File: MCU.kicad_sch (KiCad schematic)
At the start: 18 parts, among them U2 LTV-817, U3 LTV-817, Y1 TXC 7R-32.000MEEV-T

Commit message: Dodanie footprintów
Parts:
- added C11: 0.8pF, Capacitor_SMD:C_0201_0603Metric, symbol Device:C
- added C15: 0.3pF, Capacitor_SMD:C_0201_0603Metric, symbol Device:C
- added FL1: DLF162500LT-5028A1, Sterownik_roletyLibrary:DLF162500LT5028A1, symbol DLF162500LT-5028A1:DLF162500LT-5028A1
- added L1: 2.7nH, Inductor_SMD:L_0201_0603Metric, symbol Device:L
- 111111111: renamed from 1111111; footprint (none) -> Sterownik_roletyLibrary:QFN50P500X500X60-33N-D; symbol STM32WBA50KGU6:STM32WBA54KGU6 -> STM32WBA54KGU6:STM32WBA54KGU6
- C1, C10, C2, C3, C4, C5, C6, C7, C8, C9: footprint (none) -> Capacitor_SMD:C_0201_0603Metric
- C12: renamed from C11; footprint (none) -> Capacitor_SMD:C_0201_0603Metric
- C13: renamed from C12; footprint (none) -> Capacitor_SMD:C_0201_0603Metric
- C14: renamed from C13; footprint (none) -> Capacitor_SMD:C_0201_0603Metric
- Y1: footprint (none) -> Sterownik_roletyLibrary:TXC 7R-32.000MEEV-T
- renumbered U2 to U1, U3 to U2
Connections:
- net GND: now also C11.2, C15.2, FL1.2 (GND_1), FL1.4 (GND_2)
- net at 111111111.25 (RF): now also C11.1, L1.1; no longer AE1.1 (A)
- net Switch_Input_1 renamed Switch_input_1
- new net: C15.1, FL1.1 (IN), L1.2
- new net: AE1.1 (A), FL1.3 (OUT)
- no-connect marks 11 -> 13
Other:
- moved on the sheet: AE1, C12, C13, C14, Y1

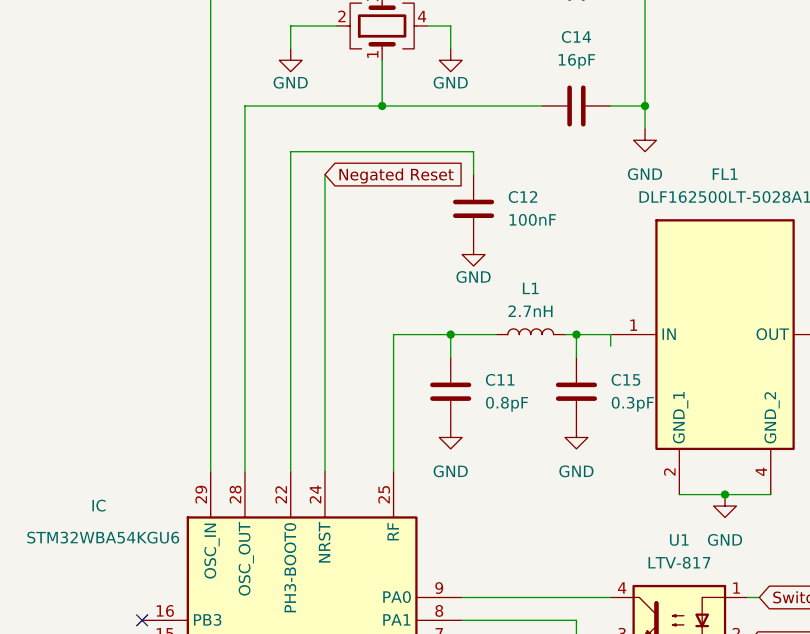
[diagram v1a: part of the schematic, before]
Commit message: początkowe rozłożenie na PCB
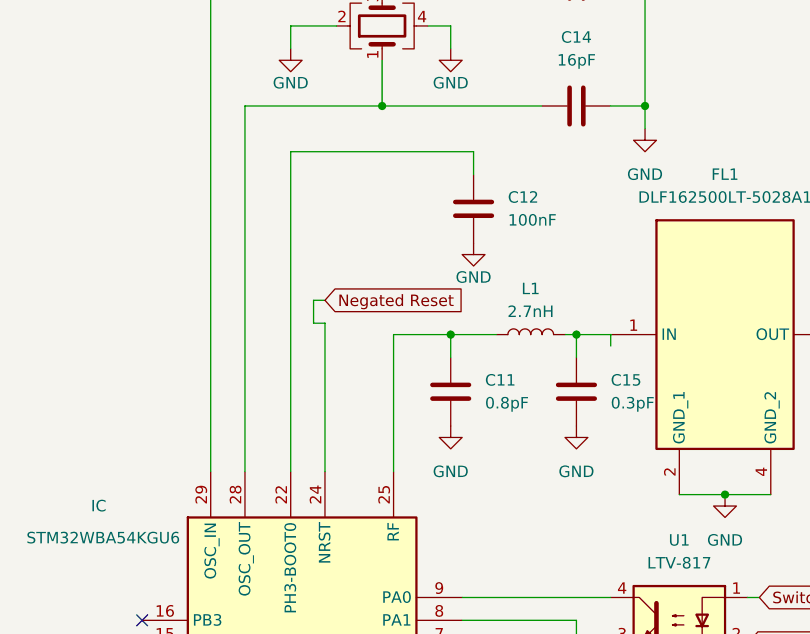
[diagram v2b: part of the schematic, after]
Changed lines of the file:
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@@
+	(wire
+		(pts
+			(xy 180.34 58.42) (xy 180.34 74.93)
+		)
+		(stroke
+			(width 0)
+			(type default)
+		)
+	)
 	(wire
 		(pts
@@
 	(wire
 		(pts
-			(xy 180.34 41.91) (xy 180.34 74.93)
-		)
-		(stroke
-			(width 0)
-			(type default)
-		)
-	)
-	(wire
-		(pts
 			(xy 62.23 138.43) (xy 62.23 147.32)
 		)
@@
 	(wire
 		(pts
+			(xy 180.34 55.88) (xy 179.07 55.88)
+		)
+		(stroke
+			(width 0)
+			(type default)
+		)
+	)
+	(wire
+		(pts
 			(xy 132.08 129.54) (xy 132.08 139.7)
 		)
@@
 	(wire
 		(pts
+			(xy 179.07 55.88) (xy 179.07 58.42)
+		)
+		(stroke
+			(width 0)
+			(type default)
+		)
+	)
+	(wire
+		(pts
 			(xy 93.98 114.3) (xy 160.02 114.3)
 		)
@@
 		(pts
 			(xy 186.69 34.29) (xy 186.69 29.21)
+		)
+		(stroke
+			(width 0)
+			(type default)
+		)
+	)
+	(wire
+		(pts
+			(xy 179.07 58.42) (xy 180.34 58.42)
 		)
 		(stroke
@@
 	(global_label "Negated Reset"
 		(shape input)
-		(at 180.34 41.91 0)
+		(at 180.34 55.88 0)
 		(fields_autoplaced yes)
 		(effects
@@
 		)
 		(property "Intersheetrefs" "${INTERSHEET_REFS}"
-			(at 197.1742 41.91 0)
+			(at 197.1742 55.88 0)
 			(effects
 				(font
